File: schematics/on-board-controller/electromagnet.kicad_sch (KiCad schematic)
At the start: 7 parts, among them Q1 NMOS, Q2 NMOS

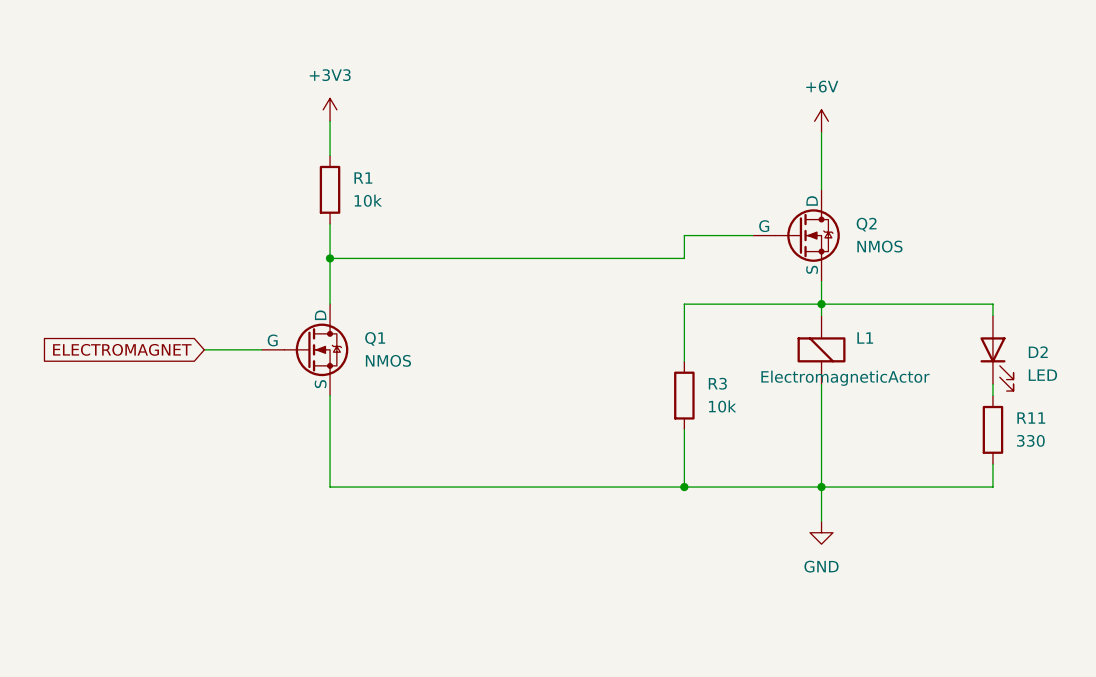
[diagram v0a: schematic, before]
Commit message: new version, and ltspice for electromagnet
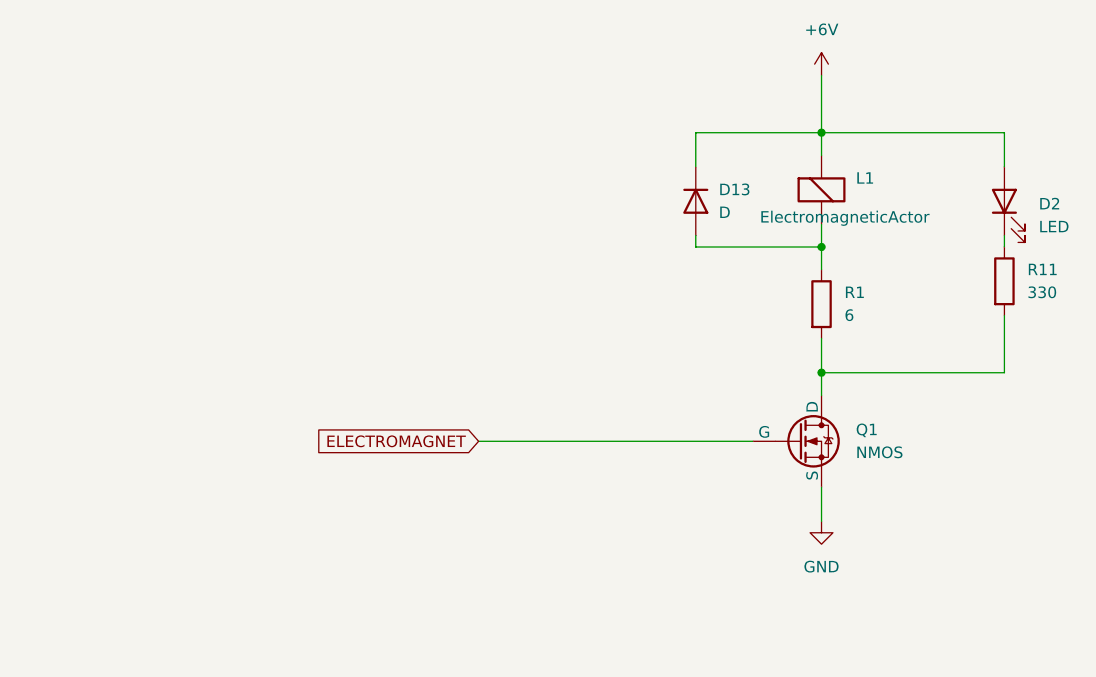
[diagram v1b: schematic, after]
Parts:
- removed Q2: NMOS, Package_TO_SOT_THT:TO-92_Inline, symbol Simulation_SPICE:NMOS
- removed R3: 10k, Resistor_SMD:R_0805_2012Metric_Pad1.20x1.40mm_HandSolder, symbol Device:R
- added D13: D, LED_SMD:LED_0805_2012Metric_Pad1.15x1.40mm_HandSolder, symbol Device:D
- R1: value 10k -> 6
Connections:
- net +6V: now also D2.2 (A), L1.1 (-), D13.1 (K)
- net GND: no longer L1.2 (+), R11.2
- net at Q1.1 (D), R1.2: now also R11.2
- net +3V3: no longer names the net of R1.1
- net +3V3: now also L1.2 (+), D13.2 (A)
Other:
- moved on the sheet: D2, L1, R11

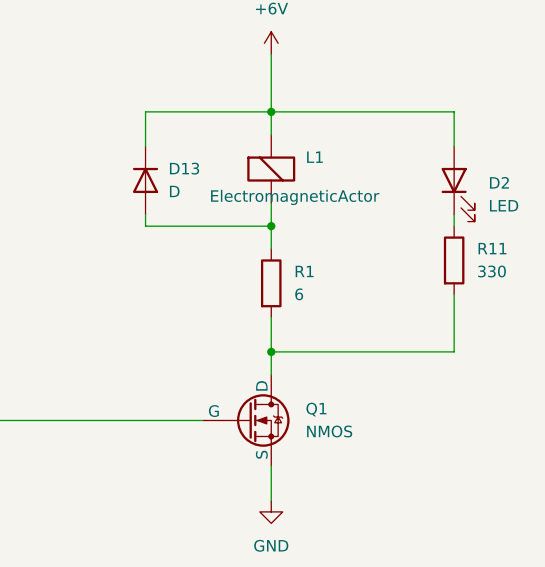
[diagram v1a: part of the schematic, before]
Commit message: changed size of electrolytic capacitors
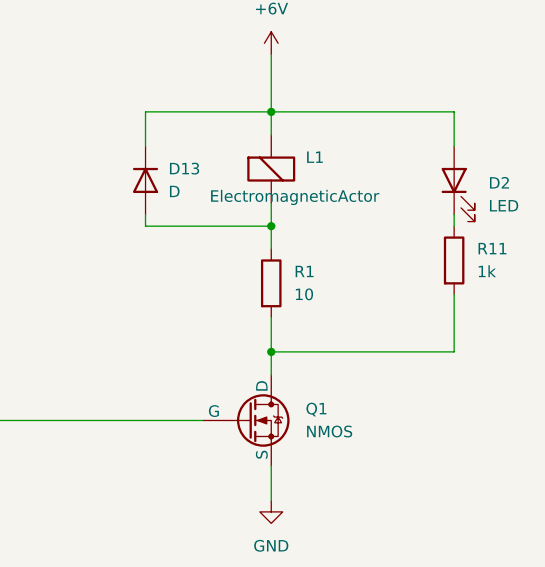
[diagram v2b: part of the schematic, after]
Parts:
- R1: value 6 -> 10
- R11: value 330 -> 1k
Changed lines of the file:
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@@
 			)
 		)
-		(property "Value" "6"
+		(property "Value" "10"
 			(at 168.91 93.9799 0)
 			(effects
@@
 			)
 		)
-		(property "Value" "330"
+		(property "Value" "1k"
 			(at 189.23 91.4399 0)
 			(effects

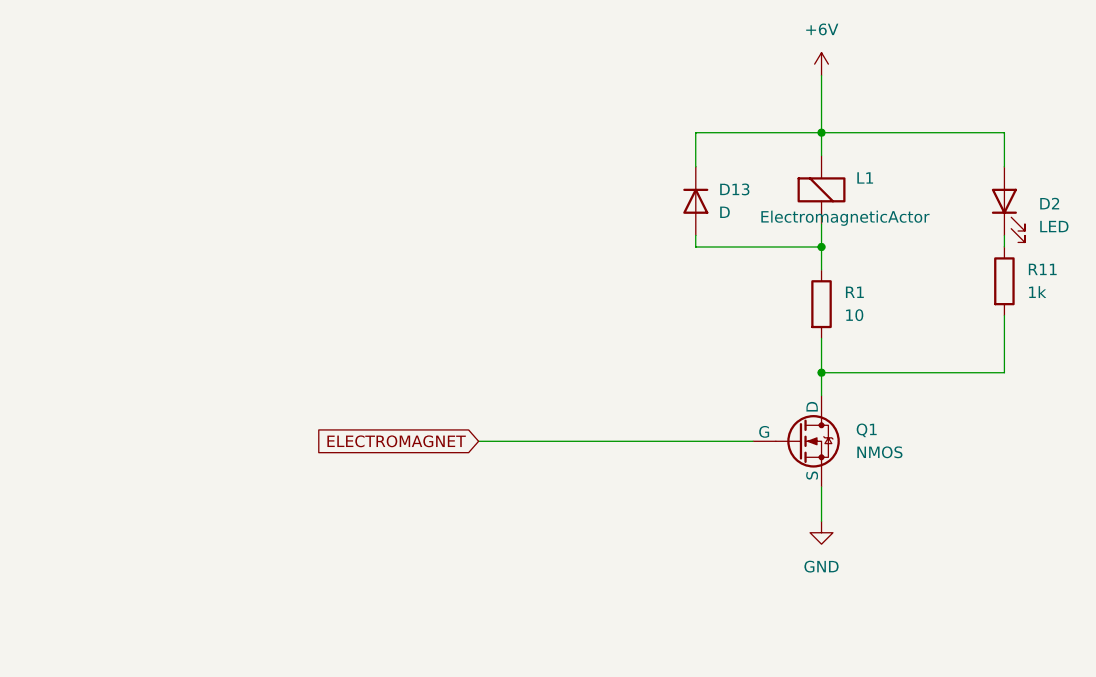
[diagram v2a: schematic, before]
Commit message: updated on-board schematic with changes
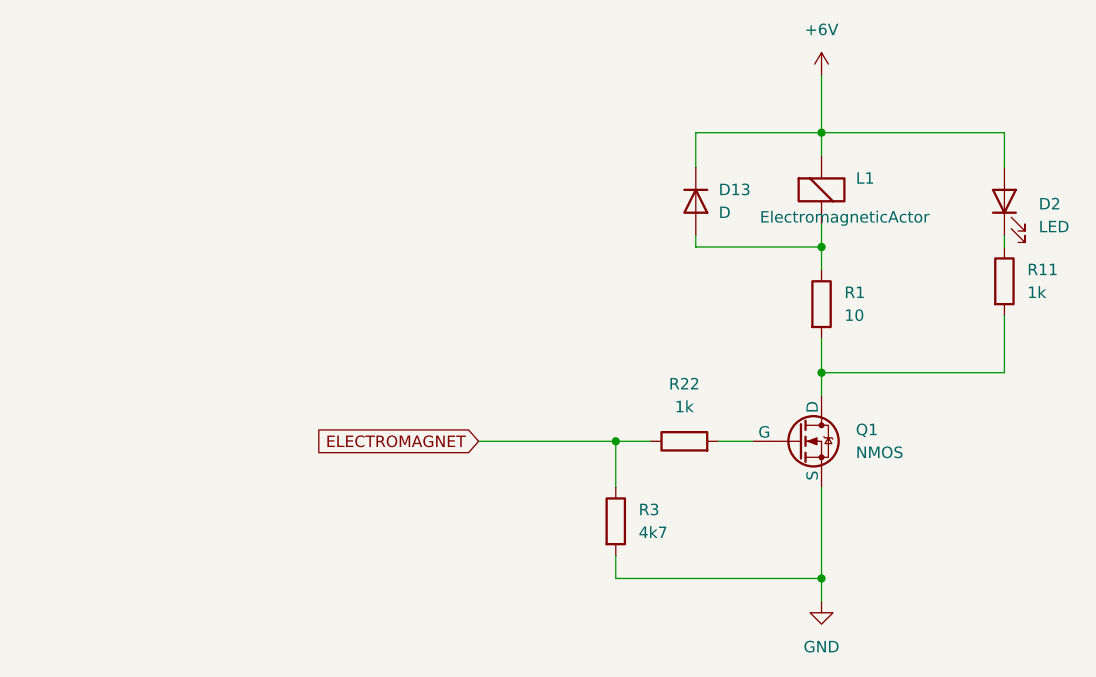
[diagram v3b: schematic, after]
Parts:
- added R22: 1k, Resistor_SMD:R_0805_2012Metric_Pad1.20x1.40mm_HandSolder, symbol Device:R
- added R3: 4k7, Resistor_SMD:R_0805_2012Metric_Pad1.20x1.40mm_HandSolder, symbol Device:R
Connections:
- net ELECTROMAGNET: now also R22.1, R3.1; no longer Q1.2 (G)
- net GND: now also R3.2
- new net: Q1.2 (G), R22.2
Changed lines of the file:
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@@
+	)
+	(junction
+		(at 143.51 107.95)
+		(diameter 0)
+		(color 0 0 0 0)
+	)
+	(junction
+		(at 166.37 123.19)
+		(diameter 0)
+		(color 0 0 0 0)
 	)
 	(junction
@@
 	(wire
 		(pts
-			(xy 128.27 107.95) (xy 158.75 107.95)
+			(xy 128.27 107.95) (xy 143.51 107.95)
+		)
+		(stroke
+			(width 0)
+			(type default)
+		)
+	)
+	(wire
+		(pts
+			(xy 143.51 120.65) (xy 143.51 123.19)
 		)
 		(stroke
@@
 	(wire
 		(pts
+			(xy 154.94 107.95) (xy 158.75 107.95)
+		)
+		(stroke
+			(width 0)
+			(type default)
+		)
+	)
+	(wire
+		(pts
 			(xy 152.4 73.66) (xy 166.37 73.66)
 		)
@@
 	(wire
 		(pts
+			(xy 143.51 107.95) (xy 147.32 107.95)
+		)
+		(stroke
+			(width 0)
+			(type default)
+		)
+	)
+	(wire
+		(pts
 			(xy 166.37 86.36) (xy 166.37 88.9)
 		)
@@
 	(wire
 		(pts
+			(xy 143.51 107.95) (xy 143.51 113.03)
+		)
+		(stroke
+			(width 0)
+			(type default)
+		)
+	)
+	(wire
+		(pts
 			(xy 186.69 93.98) (xy 186.69 100.33)
 		)
@@
 	(wire
 		(pts
-			(xy 166.37 113.03) (xy 166.37 116.84)
+			(xy 143.51 123.19) (xy 166.37 123.19)
+		)
+		(stroke
+			(width 0)
+			(type default)
+		)
+	)
+	(wire
+		(pts
+			(xy 166.37 123.19) (xy 166.37 125.73)
+		)
+		(stroke
+			(width 0)
+			(type default)
+		)
+	)
+	(wire
+		(pts
+			(xy 166.37 113.03) (xy 166.37 123.19)
 		)
 		(stroke
@@
 	(symbol
 		(lib_id "power:GND")
-		(at 166.37 116.84 0)
+		(at 166.37 125.73 0)
 		(unit 1)
 		(exclude_from_sim no)
@@
 		(fields_autoplaced yes)
 		(property "Reference" "#PWR018"
-			(at 166.37 123.19 0)
+			(at 166.37 132.08 0)
 			(effects
 				(font
@@
 		)
 		(property "Value" "GND"
-			(at 166.37 121.92 0)
+			(at 166.37 130.81 0)
 			(effects
 				(font
@@
 		)
 		(property "Footprint" ""
-			(at 166.37 116.84 0)
+			(at 166.37 125.73 0)
 			(effects
 				(font
@@
 		)
 		(property "Datasheet" ""
-			(at 166.37 116.84 0)
+			(at 166.37 125.73 0)
 			(effects
 				(font
@@
 		)
 		(property "Description" "Power symbol creates a global label with name \"GND\" , ground"
-			(at 166.37 116.84 0)
+			(at 166.37 125.73 0)
 			(effects
 				(font
@@
 	)
 	(symbol
+		(lib_id "Device:R")
+		(at 151.13 107.95 90)
+		(unit 1)
+		(exclude_from_sim no)
+		(in_bom yes)
+		(on_board yes)
+		(dnp no)
+		(fields_autoplaced yes)
+		(property "Reference" "R22"
+			(at 151.13 101.6 90)
+			(effects
+				(font
+					(size 1.27 1.27)
+				)
+			)
+		)
+		(property "Value" "1k"
+			(at 151.13 104.14 90)
+			(effects
+				(font
+					(size 1.27 1.27)
+				)
+			)
+		)
+		(property "Footprint" "Resistor_SMD:R_0805_2012Metric_Pad1.20x1.40mm_HandSolder"
+			(at 151.13 109.728 90)
+			(effects
+				(font
+					(size 1.27 1.27)
+				)
+				(hide yes)
+			)
+		)
+		(property "Datasheet" "~"
+			(at 151.13 107.95 0)
+			(effects
+				(font
+					(size 1.27 1.27)
+				)
+				(hide yes)
+			)
+		)
+		(property "Description" "Resistor"
+			(at 151.13 107.95 0)
+			(effects
+				(font
+					(size 1.27 1.27)
+				)
+				(hide yes)
+			)
+		)
+		(pin "2"
+		)
+		(pin "1"
+		)
+		(instances
+			(project "sub"
+				(path "/aba2230e-80ca-41f8-a78f-a68ad044f9a5/ba1d19a3-3ba6-428d-840f-5e7632c6e9e5"
+					(reference "R22")
+					(unit 1)
+				)
+			)
+		)
+	)
+	(symbol
 		(lib_id "power:+6V")
 		(at 166.37 67.31 0)
@@
 					(unit 1)
 				)
+			)
+		)
+	)
+	(symbol
+		(lib_id "Device:R")
+		(at 143.51 116.84 0)
+		(unit 1)
+		(exclude_from_sim no)
+		(in_bom yes)
+		(on_board yes)
+		(dnp no)
+		(fields_autoplaced yes)
+		(property "Reference" "R3"
+			(at 146.05 115.5699 0)
+			(effects
+				(font
+					(size 1.27 1.27)
+				)
+				(justify left)
+			)
+		)
+		(property "Value" "4k7"
+			(at 146.05 118.1099 0)
+			(effects
+				(font
+					(size 1.27 1.27)
+				)
+				(justify left)
+			)
+		)
+		(property "Footprint" "Resistor_SMD:R_0805_2012Metric_Pad1.20x1.40mm_HandSolder"
+			(at 141.732 116.84 90)
+			(effects
+				(font
+					(size 1.27 1.27)
+				)
+				(hide yes)
+			)
+		)
+		(property "Datasheet" "~"
+			(at 143.51 116.84 0)
+			(effects
+				(font
+					(size 1.27 1.27)
+				)
+				(hide yes)
+			)
+		)
+		(property "Description" "Resistor"
+			(at 143.51 116.84 0)
+			(effects
+				(font
+					(size 1.27 1.27)
+				)
+				(hide yes)
+			)
+		)
+		(pin "2"
+		)
+		(pin "1"
+		)
+		(instances
+			(project "sub"
+				(path "/aba2230e-80ca-41f8-a78f-a68ad044f9a5/ba1d19a3-3ba6-428d-840f-5e7632c6e9e5"
+					(reference "R3")
+					(unit 1)
+				)

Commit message: on-board: updated schematic to match STM32 confighuration
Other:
- title: sumbersible -> On-board Controller
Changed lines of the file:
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@@
 	(paper "A4")
 	(title_block
-		(title "sumbersible")
+		(title "On-board Controller")
 		(date "2024-07-16")
 		(rev "1")
